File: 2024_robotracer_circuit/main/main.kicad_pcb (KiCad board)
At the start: 2 copper layers, 60 x 60 mm, 70 parts, among them J1 PH_6p, J10 PH_5p, J11 PH_6p, J12 PH_4p, J13 PH_8p, J14 PH_6p, J2 Conn_02x05_Odd_Even, J3 Conn_02x05_Odd_Even, J4 PA_2p, J5 PA_2p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

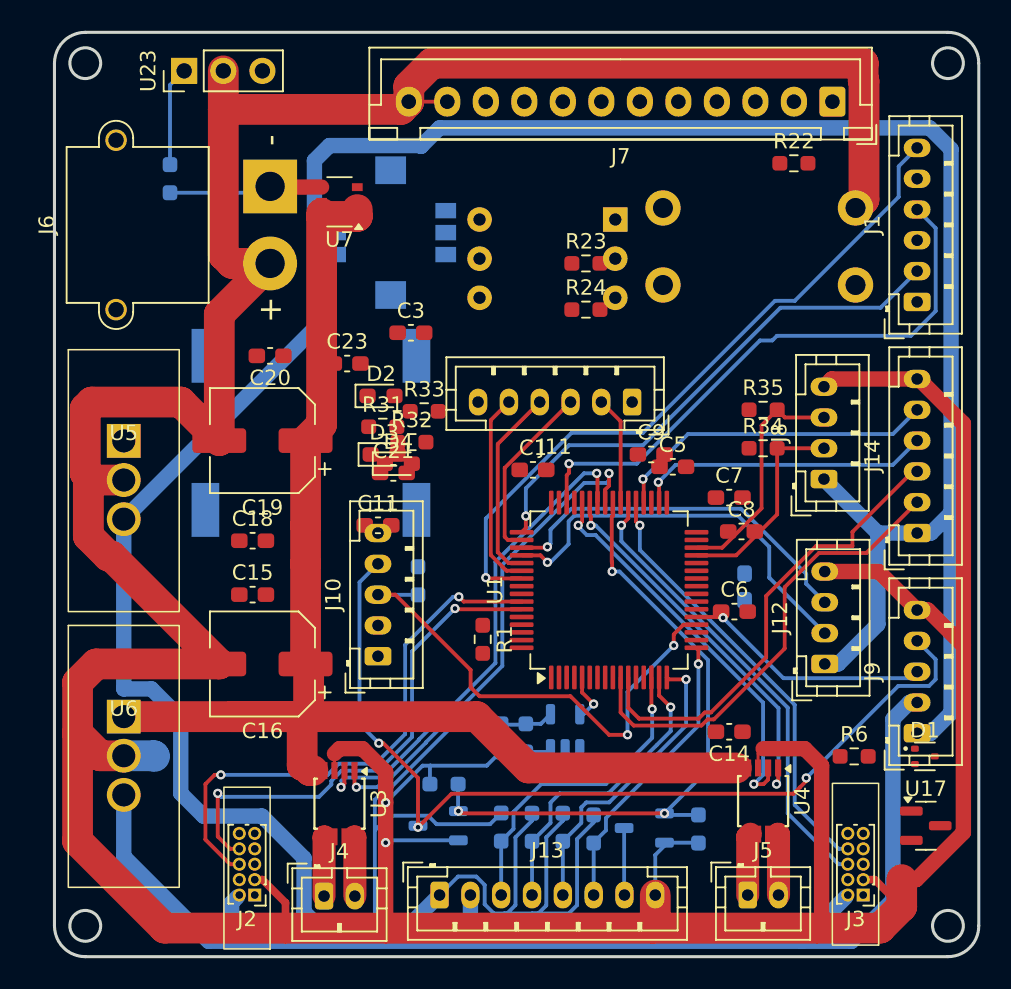
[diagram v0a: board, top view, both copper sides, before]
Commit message: マイコン回転させる前
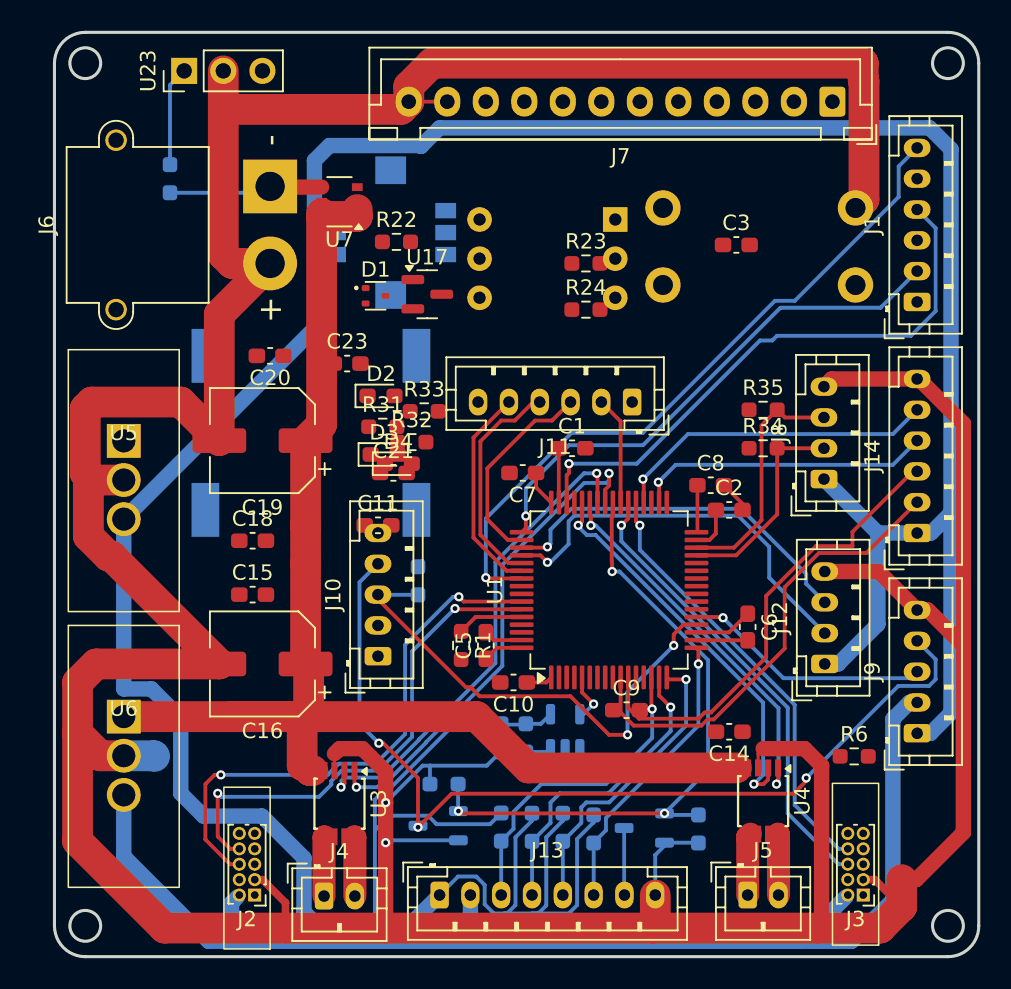
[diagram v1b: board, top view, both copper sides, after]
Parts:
- added C10: 0.1u, Capacitor_SMD:C_0603_1608Metric_Pad1.08x0.95mm_HandSolder, F.Cu at (127.8, 80.2)
- C2: moved to F.Cu
- moved U17 47.3 mm to (122.2, 55.0)
- moved D1 46.5 mm to (118.8, 55.1)
- moved R22 26.3 mm to (120.2, 51.6)
- moved C3 21.9 mm to (142.3, 51.8)
- moved C5 16.8 mm to (126.0, 77.8), turned to 90 degrees
- moved C9 16.7 mm to (135.1, 82.0)
- moved C7 13.5 mm to (128.4, 66.6), turned to 180 degrees
- moved C2 5.10 mm to (141.8, 69.0), turned to 0 degrees
- moved C8 3.61 mm to (140.6, 67.4)
- moved C1 2.90 mm to (131.6, 65.0)
- moved R1 1.46 mm to (124.4, 77.8)
- moved C6 1.32 mm to (143.0, 76.6), turned to -90 degrees
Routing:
- net +3.3V: track 239.5 -> 253.1 mm
- net GND: track 321.9 -> 329.8 mm
- net Net-(U1-BOOT0): track 0.00 -> 4.31 mm
- net Net-(U1-VCAP_2): track 0.00 -> 3.53 mm
- net Net-(U1-VCAP_1): track 0.00 -> 2.97 mm
- net /SDIO_CK: track 12.7 -> 14.4 mm
- net /SDIO_SW: track 11.7 -> 13.3 mm
- net /SDIO_CMD: track 12.8 -> 13.8 mm

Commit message: LEDつながた
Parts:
- removed J12: PH_4p, Connector_JST:JST_PH_B4B-PH-K_1x04_P2.00mm_Vertical
- removed J14: PH_6p, Connector_JST:JST_PH_B6B-PH-K_1x06_P2.00mm_Vertical
- moved C4 23.0 mm to (133.8, 61.8)
- moved R4 23.0 mm to (135.3, 61.8)
- moved U2 23.0 mm to (137.9, 61.4)
- moved J11 20.4 mm to (154.0, 70.6), turned to 90 degrees
- moved C9 11.3 mm to (126.0, 75.4)
- moved C8 9.69 mm to (144.2, 76.4)
- moved C2 9.31 mm to (144.2, 78.0)
- moved U1 5.14 mm to (135.2, 69.2), turned to -90 degrees
- moved R1 4.80 mm to (124.5, 73.0)
- moved C3 4.66 mm to (137.6, 51.7)
- moved C10 4.57 mm to (131.1, 77.0)
- moved C5 4.40 mm to (126.1, 73.4)
- moved C1 3.40 mm to (131.6, 61.6)
- moved C7 2.83 mm to (128.0, 63.8)
- moved R34 2.72 mm to (144.8, 67.6), turned to 90 degrees
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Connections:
- J8 pad 2: /LCD_SCL -> /LCD_SDA
- J8 pad 3: /LCD_SDA -> /LCD_SCL
- R34 pad 2: /LCD_SCL -> /LCD_SDA
- R35 pad 2: /LCD_SDA -> /LCD_SCL
- U1 pad 10: /SPI_MISO_GP -> unconnected-(U1-PC2-Pad10)
- U1 pad 11: /SPI_MOSI_GP -> unconnected-(U1-PC3-Pad11)
- U1 pad 14: /SENSOR0_ADC -> /SENSOR3_ADC
- U1 pad 15: /SENSOR1_ADC -> /SENSOR2_ADC
- U1 pad 16: /SENSOR2_ADC -> /SENSOR1_ADC
- U1 pad 17: /SENSOR3_ADC -> /SENSOR0_ADC
- U1 pad 2: /LED2 -> /LED3
- U1 pad 23: /SW_A -> /SW_B
- U1 pad 24: /SW_B -> /SW_A
- U1 pad 26: /SW_C -> /SW_D
- U1 pad 27: /SW_D -> /SW_C
- U1 pad 3: /LED3 -> /LED4
- U1 pad 33: /LED5 -> /LED9
- U1 pad 34: /SPI_SCK_GP -> unconnected-(U1-PB13-Pad34)
- U1 pad 36: /PWM_GP -> unconnected-(U1-PB15-Pad36)
- U1 pad 37: /ENC2_B -> /ENC1_A
- U1 pad 38: /ENC2_A -> /ENC1_B
- U1 pad 4: /LED4 -> /LED5
- U1 pad 41: /MOTOR1_IN_A -> /MOTOR1_IN_B
- U1 pad 42: /MOTOR1_IN_B -> /MOTOR1_IN_A
- U1 pad 43: /MOTOR2_IN_A -> /MOTOR2_IN_B
- U1 pad 44: /MOTOR2_IN_B -> /MOTOR2_IN_A
- U1 pad 45: /LED9 -> /LED0
- U1 pad 51: /USART_TX -> unconnected-(U1-PC10-Pad51)
- U1 pad 52: /USART_RX -> unconnected-(U1-PC11-Pad52)
- U1 pad 56: /LED7 -> /LED1
- U1 pad 57: /LED6 -> /LED2
- U1 pad 58: /ENC1_A -> /ENC2_A
- U1 pad 59: /ENC1_B -> /ENC2_B
- U1 pad 8: /LED0 -> /LED6
- U1 pad 9: /LED1 -> /LED7
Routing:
- net /LED0: track 0.00 -> 65.4 mm
- net /LED9: track 0.00 -> 42.7 mm
- net +3.3V: track 253.1 -> 212.3 mm
- net GND: track 329.8 -> 289.2 mm
- net /LED8: track 0.00 -> 34.2 mm
- net /LED1: track 0.00 -> 33.9 mm
- net /LED2: track 0.00 -> 32.6 mm
- net /SPI_MOSI_GP: track 30.5 -> 0.00 mm
- net /SPI_MISO_GP: track 30.2 -> 0.00 mm
- net /LED7: track 0.00 -> 29.3 mm
- net /LED6: track 0.00 -> 28.3 mm
- net /LED3: track 0.00 -> 27.4 mm
- net /LED5: track 0.00 -> 26.9 mm
- net /SW_B: track 0.00 -> 26.8 mm, vias 0 -> 1
- net /SDIO_D0: track 7.04 -> 33.9 mm, vias 0 -> 1
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
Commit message: 未配線はなし
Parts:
- C1, C18, C21, C6, R1, R23, R24, R6: moved to B.Cu
- moved C21 30.0 mm to (101.5, 90.3), turned to 180 degrees
- moved R33 29.7 mm to (107.1, 88.3), turned to -90 degrees
- moved D4 29.1 mm to (107.1, 91.9), turned to 90 degrees
- moved C20 25.4 mm to (112.6, 84.4)
- moved C10 18.7 mm to (140.9, 61.1), turned to 0 degrees
- moved C2 18.6 mm to (126.4, 72.6), turned to 180 degrees
- moved C11 18.0 mm to (113.6, 87.2), turned to -90 degrees
- moved R32 15.2 mm to (107.1, 70.4), turned to -90 degrees
- moved R1 15.0 mm to (138.0, 66.5), turned to 90 degrees
- moved D3 15.0 mm to (107.1, 73.9), turned to 90 degrees
- moved R22 14.6 mm to (121.2, 66.2), turned to 180 degrees
- moved R24 14.5 mm to (129.4, 70.2), turned to -90 degrees
- moved R23 13.9 mm to (129.4, 66.5), turned to -90 degrees
- moved C1 12.6 mm to (138.4, 72.2), turned to 90 degrees
- moved C6 12.6 mm to (141.4, 63.6), turned to 0 degrees
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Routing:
- net GND: track 289.2 -> 532.1 mm, vias 2 -> 18
- net +3.3V: track 212.3 -> 363.8 mm, vias 0 -> 10
- net +BATT: track 86.1 -> 139.5 mm, vias 0 -> 2
- net +5V: track 67.3 -> 114.5 mm, vias 0 -> 3
- net /BZ_PWM: track 0.00 -> 23.1 mm
- net Net-(J1-Pin_5): track 17.3 -> 36.2 mm, vias 0 -> 2
- net /ENC2_B: track 10.9 -> 29.1 mm, vias 1 -> 3
- net /ENC2_A: track 12.8 -> 30.0 mm, vias 1 -> 3
- net Net-(J10-Pin_4): track 46.1 -> 61.7 mm, vias 3 -> 4
- net Net-(U7-GATE): track 6.47 -> 17.0 mm, vias 0 -> 1
- net /SENSOR_R_ADC: track 33.1 -> 41.3 mm
- net Net-(BZ1--): track 0.00 -> 7.53 mm, vias 0 -> 1
- net /LED7: track 29.3 -> 22.7 mm
- net /BATT_REF_ADC: track 0.00 -> 5.54 mm, vias 0 -> 1
- net /SENSOR_PWM: track 37.8 -> 32.7 mm
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
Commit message: べた
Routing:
- added copper zone on B.Cu, net GND
- added copper zone on F.Cu, net GND
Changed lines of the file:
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@@
 		(net 87)
+	)
+	(zone
+		(net 2)
+		(net_name "GND")
+		(layers "F&B.Cu")
+		(hatch edge 0.5)
+		(connect_pads
+			(clearance 0.5)
+		)
+		(min_thickness 0.25)
+		(filled_areas_thickness no)
+		(fill yes
+			(thermal_gap 0.5)
+			(thermal_bridge_width 0.5)
+		)
+		(polygon
+			(pts
+				(xy 98 38) (xy 158 37.9) (xy 158 98) (xy 98 98)
+			)
+		)
 	)
 	(group ""

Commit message: エラーなし
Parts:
- added G***: LOGO, mylib:SH_5mm, F.Cu at (154.9, 90.0)
- moved C4 5.18 mm to (137.8, 56.9), turned to 180 degrees
- moved R35 0.90 mm to (143.9, 64.0)
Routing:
- net GND: track 532.1 -> 541.2 mm, vias 18 -> 114
- net +3.3V: track 363.8 -> 370.7 mm
- net Net-(J6-Pin_1): track 11.5 -> 15.1 mm
- net /IMU_SCL: track 21.2 -> 24.7 mm
- net +5V: track 114.5 -> 116.3 mm
- net /IMU_SDA: track 24.4 -> 25.8 mm
- net /LED2: track 32.2 -> 33.3 mm
- net /LED4: track 26.1 -> 25.1 mm
- net /LED3: track 25.3 -> 24.3 mm
- net /LED1: track 34.6 -> 35.5 mm
- net /SW_D: track 26.0 -> 26.8 mm
- net /LED5: track 26.9 -> 26.2 mm

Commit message: 修正
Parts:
- R23: value R_Small -> 1.8k
- R24: value R_Small -> 1k
- U16: moved to F.Cu
- U3, U4: footprint Package_SO:TSSOP-8_3x3mm_P0.65mm -> Package_SO:SOP-8_3.9x4.9mm_P1.27mm
- moved C14 0.87 mm to (140.3, 84.0)
- moved C20 0.80 mm to (111.8, 84.4)
- moved C11 0.71 mm to (112.9, 87.1)
- moved D1 0.45 mm to (117.9, 66.0), turned to -90 degrees
- moved U16 0.30 mm to (130.0, 53.3), turned to 0 degrees
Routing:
- net GND: track 541.2 -> 522.3 mm, vias 114 -> 115
- net /IMU_SDA: track 25.8 -> 35.1 mm, vias 1 -> 2
- net /IMU_SCL: track 24.7 -> 33.6 mm, vias 1 -> 2
- net /LED8: track 34.2 -> 36.4 mm
- net +3.3V: track 370.7 -> 369.3 mm, vias 10 -> 9
- net Net-(J10-Pin_4): track 61.5 -> 62.8 mm
- net +BATT: track 139.5 -> 140.6 mm
- net Net-(J5-Pin_2): track 3.96 -> 4.99 mm
- net Net-(J4-Pin_1): track 3.86 -> 4.75 mm
- net Net-(J5-Pin_1): track 4.02 -> 4.89 mm
- net /MOTOR2_IN_A: track 19.7 -> 20.6 mm

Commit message: 修正
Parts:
- moved C4 2.57 mm to (135.3, 57.5)
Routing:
- net +3.3V: track 369.3 -> 371.8 mm
- net Net-(J1-Pin_5): track 36.2 -> 37.2 mm
- net GND: track 522.3 -> 523.2 mm
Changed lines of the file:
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@@
 	(footprint "Capacitor_SMD:C_0603_1608Metric_Pad1.08x0.95mm_HandSolder"
 		(layer "B.Cu")
-		(at 137.8 56.9 180)
+		(at 135.3 57.5 180)
 		(descr "Capacitor SMD 0603 (1608 Metric), square (rectangular) end terminal, IPC_7351 nominal with elongated pad for handsoldering. (Body size source: IPC-SM-782 page 76, https://www.pcb-3d.com/wordpress/wp-content/uploads/ipc-sm-782a_amendment_1_and_2.pdf), generated with kicad-footprint-generator")
 		(tags "capacitor handsolder")
@@
 	)
 	(segment
-		(start 136.9375 58.178616)
-		(end 136.9375 56.9)
-		(width 0.25)
-		(layer "B.Cu")
-		(net 2)
-	)
-	(segment
 		(start 122.375 86.8)
 		(end 122.375 86.175)
@@
 	)
 	(segment
-		(start 122.1 85.9)
-		(end 121.6 85.9)
-		(width 0.25)
-		(layer "B.Cu")
-		(net 2)
-	)
-	(segment
-		(start 147.2 59.7)
-		(end 148 60.5)
+		(start 134.436244 57.501256)
+		(end 130.698744 57.501256)
 		(width 0.25)
 		(layer "B.Cu")
@@
 	)
 	(segment
-		(start 137.9375 55.9)
-		(end 136.9375 56.9)
+		(start 122.1 85.9)
+		(end 121.6 85.9)
 		(width 0.25)
 		(layer "B.Cu")
@@
 	)
 	(segment
-		(start 139.716116 55.9)
-		(end 137.9375 55.9)
+		(start 147.2 59.7)
+		(end 148 60.5)
 		(width 0.25)
 		(layer "B.Cu")
@@
 	)
 	(segment
-		(start 136.786396 56.9)
-		(end 136.18514 57.501256)
+		(start 136.0375 55.9)
+		(end 134.4375 57.5)
 		(width 0.25)
 		(layer "B.Cu")
@@
 	)
 	(segment
+		(start 141.958058 58.141942)
+		(end 139.716116 55.9)
+		(width 0.25)
+		(layer "B.Cu")
+		(net 2)
+	)
+	(segment
 		(start 139.775 90.6)
 		(end 139.8 90.625)
@@
 	)
 	(segment
+		(start 134.4375 57.5)
+		(end 136.1375 59.2)
+		(width 0.25)
+		(layer "B.Cu")
+		(net 2)
+	)
+	(segment
 		(start 111.1 59.6)
 		(end 116.3 59.6)
@@
 	)
 	(segment
-		(start 141.958058 58.141942)
-		(end 139.716116 55.9)
-		(width 0.25)
-		(layer "B.Cu")
-		(net 2)
-	)
-	(segment
-		(start 136.9 59.2)
-		(end 136.9 58.216116)
-		(width 0.25)
-		(layer "B.Cu")
-		(net 2)
-	)
-	(segment
 		(start 117.3 60.6)
 		(end 117.6 60.6)
@@
 	)
 	(segment
-		(start 136.18514 57.501256)
-		(end 130.698744 57.501256)
-		(width 0.25)
-		(layer "B.Cu")
-		(net 2)
-	)
-	(segment
 		(start 140.6 76.740225)
 		(end 148.159775 76.740225)
@@
 	)
 	(segment
-		(start 136.9 58.216116)
-		(end 136.9375 58.178616)
+		(start 142.225 63.6)
+		(end 142.225 65.75)
 		(width 0.25)
 		(layer "B.Cu")
@@
 	)
 	(segment
-		(start 142.225 63.6)
-		(end 142.225 65.75)
+		(start 134.4375 57.5)
+		(end 134.436244 57.501256)
 		(width 0.25)
 		(layer "B.Cu")
@@
 	)
 	(segment
+		(start 136.1375 59.2)
+		(end 136.9 59.2)
+		(width 0.25)
+		(layer "B.Cu")
+		(net 2)
+	)
+	(segment
 		(start 137 91.4)
 		(end 137 94)
@@
 	)
 	(segment
+		(start 130.698744 57.501256)
+		(end 130 58.2)
+		(width 0.25)
+		(layer "B.Cu")
+		(net 2)
+	)
+	(segment
 		(start 122.375 86.175)
 		(end 122.1 85.9)
@@
 	)
 	(segment
-		(start 136.9375 56.9)
-		(end 136.786396 56.9)
-		(width 0.25)
-		(layer "B.Cu")
-		(net 2)
-	)
-	(segment
-		(start 130.698744 57.501256)
-		(end 130 58.2)
+		(start 139.716116 55.9)
+		(end 136.0375 55.9)
 		(width 0.25)
 		(layer "B.Cu")
@@
 	)
 	(segment
+		(start 135.052816 58.999696)
+		(end 141.4 52.652512)
+		(width 0.25)
+		(layer "F.Cu")
+		(net 4)
+	)
+	(segment
 		(start 140 50.575)
 		(end 138.675 50.575)
@@
 	)
 	(segment
-		(start 135.95 61.825)
-		(end 135.95 63.525)
+		(start 134.867465 58.999696)
+		(end 135.052816 58.999696)
 		(width 0.25)
 		(layer "F.Cu")
@@
 	)
 	(segment
-		(start 141.4 52.652512)
-		(end 135.926256 58.126256)
+		(start 135.95 61.825)
+		(end 135.95 63.525)
 		(width 0.25)
 		(layer "F.Cu")
@@
 	)
 	(segment
-		(start 140 50.575)
+		(start 141.4 52.652512)
 		(end 141.4 51.975)
 		(width 0.25)
@@
 	(segment
 		(start 141.4 51.975)
-		(end 141.4 52.652512)
+		(end 140 50.575)
 		(width 0.25)
 		(layer "F.Cu")
@@
 	)
 	(via
-		(at 135.926256 58.126256)
+		(at 134.867465 58.999696)
 		(size 0.6)
 		(drill 0.3)
@@
 	)
 	(segment
+		(start 134.867465 58.999696)
+		(end 135.926256 60.058487)
+		(width 0.25)
+		(layer "B.Cu")
+		(net 4)
+	)
+	(segment
 		(start 139.4 47.5)
 		(end 154 47.5)
@@
 	)
 	(segment
-		(start 135.926256 58.126256)
+		(start 135.926256 60.058487)
 		(end 135.926256 61.551256)
 		(width 0.25)
@@
 	)
 	(segment
+		(start 139.964576 57.3)
+		(end 142.564576 59.9)
+		(width 0.25)
+		(layer "B.Cu")
+		(net 5)
+	)
+	(segment
 		(start 150.7 81.9125)
 		(end 152.1125 81.9125)
@@
 	)
 	(segment
-		(start 138.6625 56.9)
-		(end 139.564576 56.9)
-		(width 0.25)
-		(layer "B.Cu")
-		(net 5)
-	)
-	(segment
 		(start 126.525 95.2)
 		(end 125.925 94.6)
@@
 	)
 	(segment
+		(start 142.564576 59.9)
+		(end 142.775 59.9)
+		(width 0.25)
+		(layer "B.Cu")
+		(net 5)
+	)
+	(segment
 		(start 127 88.675)
 		(end 126.275 89.4)
@@
 	)
 	(segment
+		(start 136.1625 57.5)
+		(end 136.3625 57.3)
+		(width 0.25)
+		(layer "B.Cu")
+		(net 5)
+	)
+	(segment
 		(start 107.95 55.45)
 		(end 107.95 46.85)
@@
 	)
 	(segment
-		(start 142.564576 59.9)
-		(end 142.775 59.9)
-		(width 0.25)
-		(layer "B.Cu")
-		(net 5)
-	)
-	(segment
 		(start 134.105 55.23)
 		(end 128.87 55.23)
@@
 	)
 	(segment
+		(start 136.3625 57.3)
+		(end 139.964576 57.3)
+		(width 0.25)
+		(layer "B.Cu")
+		(net 5)
+	)
+	(segment
 		(start 114.90457 95.8)
 		(end 120 95.8)
@@
 	)
 	(segment
-		(start 139.564576 56.9)
-		(end 142.564576 59.9)
-		(width 0.25)
-		(layer "B.Cu")
-		(net 5)
-	)
-	(segment
 		(start 125.925 93.341852)
 		(end 125.383148 92.8)
@@
 	)
 	(segment
-		(start 132.1 56.5)
-		(end 134.95 59.35)
+		(start 134.158884 59.175)
+		(end 134.95 59.966116)
 		(width 0.25)
 		(layer "F.Cu")
@@
 	)
 	(segment
-		(start 132.1 43.6)
-		(end 132.1 56.5)
+		(start 131 42.5)
+		(end 132.1 43.6)
 		(width 0.25)
 		(layer "F.Cu")
@@
 	)
 	(segment
-		(start 131 42.5)
-		(end 132.1 43.6)
+		(start 132.1 57.6)
+		(end 133.675 59.175)
+		(width 0.25)
+		(layer "F.Cu")
+		(net 63)
+	)
+	(segment
+		(start 133.675 59.175)
+		(end 134.158884 59.175)
 		(width 0.25)
 		(layer "F.Cu")
@@
 	)
 	(segment
-		(start 134.95 59.35)
+		(start 134.95 59.966116)
 		(end 134.95 63.525)
 		(width 0.25)
 		(layer "F.Cu")
+		(net 63)
+	)
+	(segment
+		(start 132.1 43.6)
+		(end 132.1 57.6)
+		(width 0.25)
+		(layer "F.Cu")
